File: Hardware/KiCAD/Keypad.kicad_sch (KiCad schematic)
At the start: 0 parts

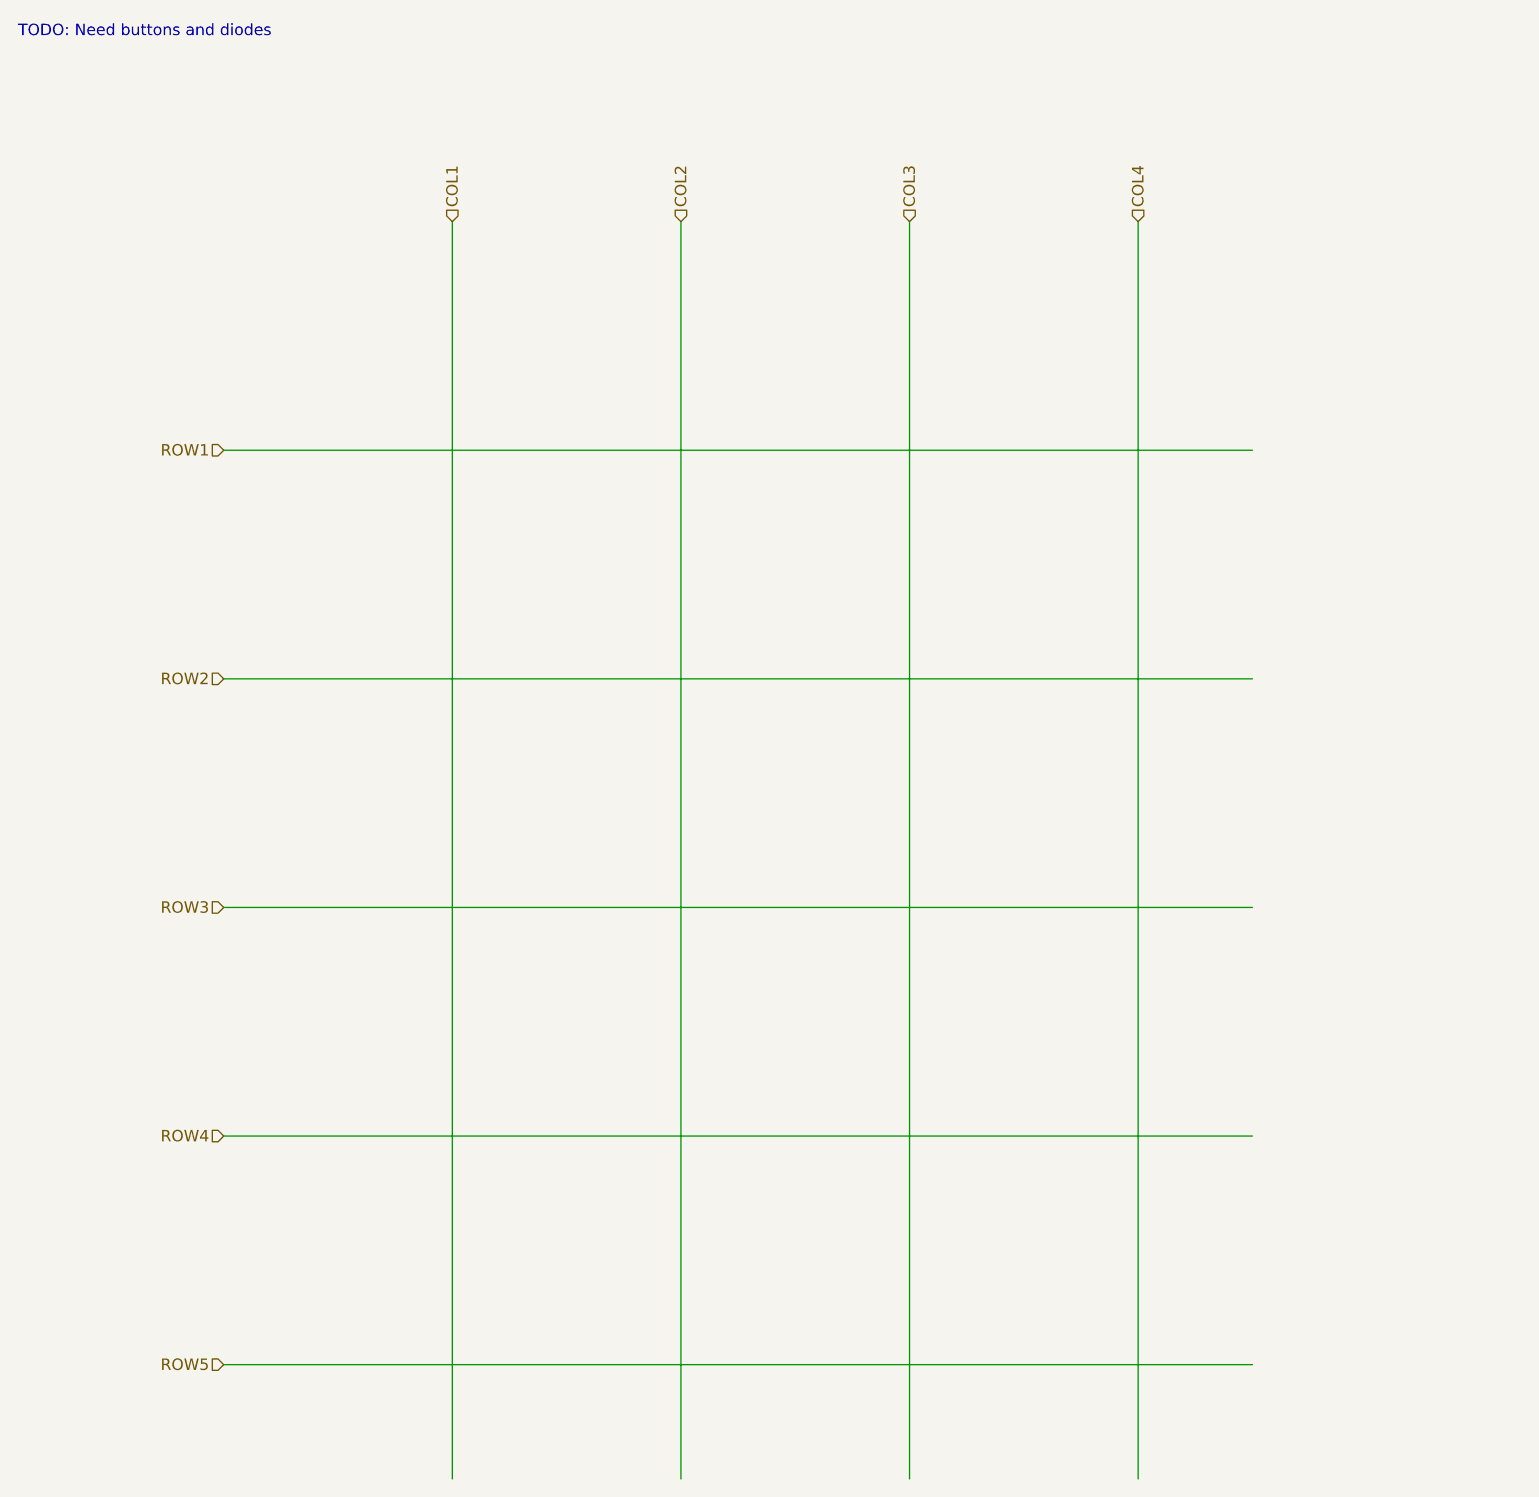
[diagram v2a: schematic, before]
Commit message: feat: subsystem exploration, begin placement, routing #11 #12 #4 many new project symbols
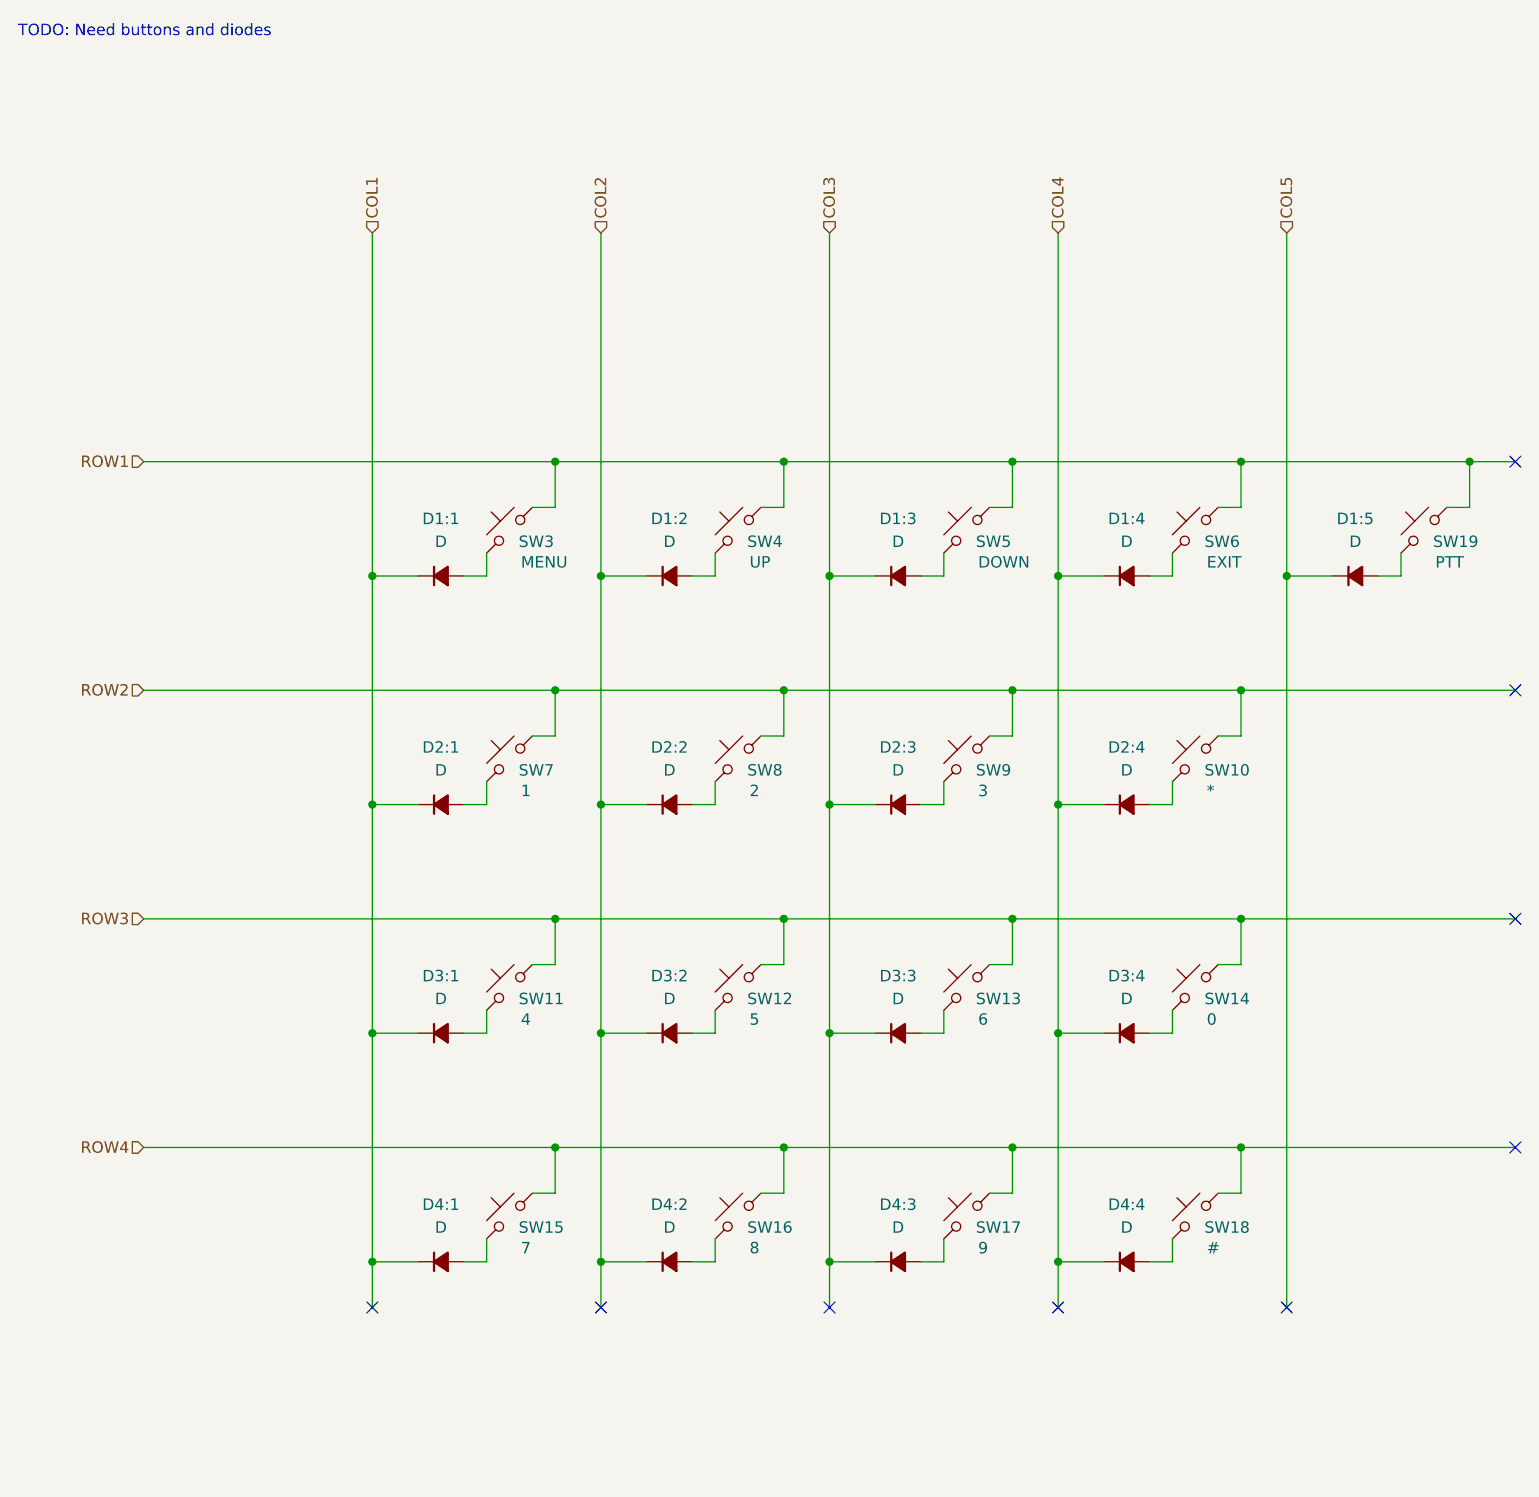
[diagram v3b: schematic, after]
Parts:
- added D1:1, D1:2, D1:3, D1:4, D1:5, D2:1, D2:2, D2:3, D2:4, D3:1, D3:2, D3:3, D3:4, D4:1, D4:2, D4:3, D4:4: D, Diode_SMD:D_0603_1608Metric, symbol Device:D_Small_Filled
- added SW10: *, Button_Switch_THT:SW_PUSH_6mm_H7.3mm, symbol Switch:SW_Push_45deg
- added SW11: 4, Button_Switch_THT:SW_PUSH_6mm_H7.3mm, symbol Switch:SW_Push_45deg
- added SW12: 5, Button_Switch_THT:SW_PUSH_6mm_H7.3mm, symbol Switch:SW_Push_45deg
- added SW13: 6, Button_Switch_THT:SW_PUSH_6mm_H7.3mm, symbol Switch:SW_Push_45deg
- added SW14: 0, Button_Switch_THT:SW_PUSH_6mm_H7.3mm, symbol Switch:SW_Push_45deg
- added SW15: 7, Button_Switch_THT:SW_PUSH_6mm_H7.3mm, symbol Switch:SW_Push_45deg
- added SW16: 8, Button_Switch_THT:SW_PUSH_6mm_H7.3mm, symbol Switch:SW_Push_45deg
- added SW17: 9, Button_Switch_THT:SW_PUSH_6mm_H7.3mm, symbol Switch:SW_Push_45deg
- added SW18: #, Button_Switch_THT:SW_PUSH_6mm_H7.3mm, symbol Switch:SW_Push_45deg
- added SW19: PTT, Button_Switch_THT:SW_PUSH_6mm_H7.3mm, symbol Switch:SW_Push_45deg
- added SW3: MENU, Button_Switch_THT:SW_PUSH_6mm_H7.3mm, symbol Switch:SW_Push_45deg
- added SW4: UP, Button_Switch_THT:SW_PUSH_6mm_H7.3mm, symbol Switch:SW_Push_45deg
- added SW5: DOWN, Button_Switch_THT:SW_PUSH_6mm_H7.3mm, symbol Switch:SW_Push_45deg
- added SW6: EXIT, Button_Switch_THT:SW_PUSH_6mm_H7.3mm, symbol Switch:SW_Push_45deg
- added SW7: 1, Button_Switch_THT:SW_PUSH_6mm_H7.3mm, symbol Switch:SW_Push_45deg
- added SW8: 2, Button_Switch_THT:SW_PUSH_6mm_H7.3mm, symbol Switch:SW_Push_45deg
- added SW9: 3, Button_Switch_THT:SW_PUSH_6mm_H7.3mm, symbol Switch:SW_Push_45deg
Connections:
- net COL1: now also D1:1.1 (K), D2:1.1 (K), D3:1.1 (K), D4:1.1 (K)
- net COL2: now also D1:2.1 (K), D2:2.1 (K), D3:2.1 (K), D4:2.1 (K)
- net COL3: now also D1:3.1 (K), D2:3.1 (K), D3:3.1 (K), D4:3.1 (K)
- net COL4: now also D1:4.1 (K), D2:4.1 (K), D3:4.1 (K), D4:4.1 (K)
- net ROW1: now also SW19.2, SW3.2, SW4.2, SW5.2, SW6.2
- net ROW2: now also SW10.2, SW7.2, SW8.2, SW9.2
- net ROW3: now also SW11.2, SW12.2, SW13.2, SW14.2
- net ROW4: now also SW15.2, SW16.2, SW17.2, SW18.2
- new net: D2:2.2 (A), SW8.1
- new net: D4:1.2 (A), SW15.1
- new net: D4:3.2 (A), SW17.1
- new net: D2:1.2 (A), SW7.1
- new net: D1:5.2 (A), SW19.1
- new net: D2:3.2 (A), SW9.1
- new net: D1:1.2 (A), SW3.1
- new net: D4:2.2 (A), SW16.1
- new net: D3:1.2 (A), SW11.1
- new net: D1:2.2 (A), SW4.1
- new net: D2:4.2 (A), SW10.1
- new net: D4:4.2 (A), SW18.1
- new net: D3:2.2 (A), SW12.1
- new net: D1:4.2 (A), SW6.1
- new net: D1:3.2 (A), SW5.1
- new net: D3:3.2 (A), SW13.1
- new net: D3:4.2 (A), SW14.1
- new net COL5: D1:5.1 (K)
- no-connect marks 0 -> 9
